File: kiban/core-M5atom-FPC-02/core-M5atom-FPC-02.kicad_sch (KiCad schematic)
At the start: 18 parts, among them J12 TP_VIN, J13 TP_3V3, J14 TP_PGND, J15 TP_PGND, J16 ESP32-01, J17 ESP32-01, J18 TP_PGND, J3 M5atom-L, J4 M5atomS3-R, J5 3V3, J6 5V, J9 I2C, U1 AE-BNO055

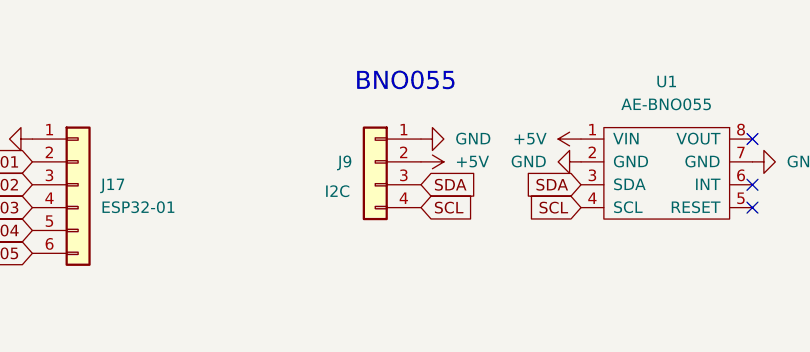
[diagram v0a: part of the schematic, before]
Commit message: kiban: rename core-M5atom-FPC−02 → core-M5atom-FPC-02 (ASCII hyphen)
Directory and filenames used U+2212 MINUS SIGN instead of ASCII '-',
which rendered as a multi-byte character on GitHub. Pure rename, no
content change.

Co-Authored-By: Claude Opus 5 <noreply@anthropic.com>
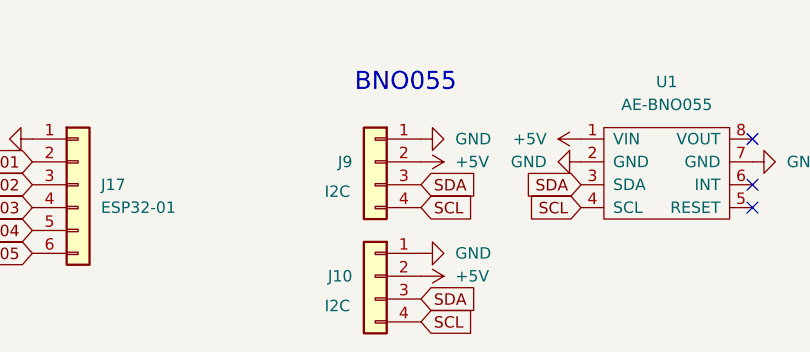
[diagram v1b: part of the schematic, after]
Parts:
- added J10: I2C, Connector_PinHeader_2.00mm:PinHeader_1x04_P2.00mm_Vertical, symbol Connector_Generic:Conn_01x04
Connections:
- net +5V: now also J10.2 (Pin_2)
- net GND: now also J10.1 (Pin_1)
- net SCL: now also J10.4 (Pin_4)
- net SDA: now also J10.3 (Pin_3)
